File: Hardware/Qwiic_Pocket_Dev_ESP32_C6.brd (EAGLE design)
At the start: 25.4 x 25.4 mm, 94 parts, among them J1 USB Female Type C Connector, J4 QWIIC_RIGHT_ANGLE, Q1 20V/4.2A/52mΩ/1.4W, U1 ESP32-C6-MINI-1, U2 RT9080-33GJ5, U3 MCP73831

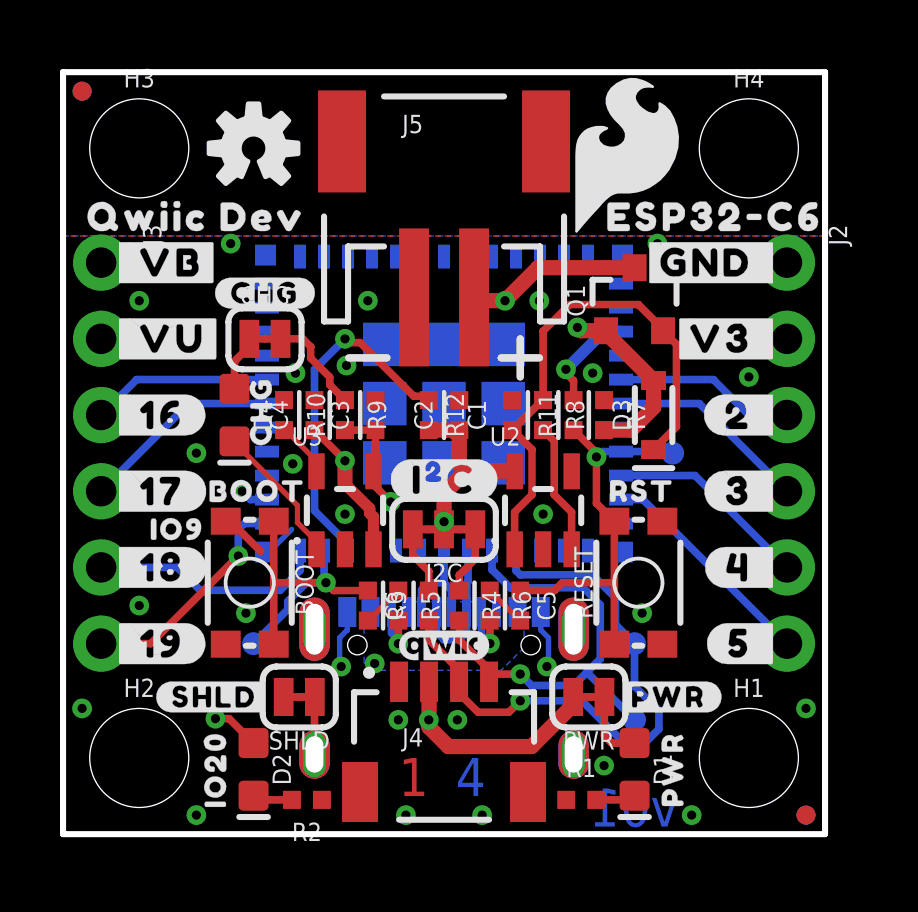
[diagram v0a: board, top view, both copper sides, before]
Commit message: Move fiducials
Moved inward to make it easier for PnP to handle single boards
Decided to flip the fiducial corners, made it easier to move inwards
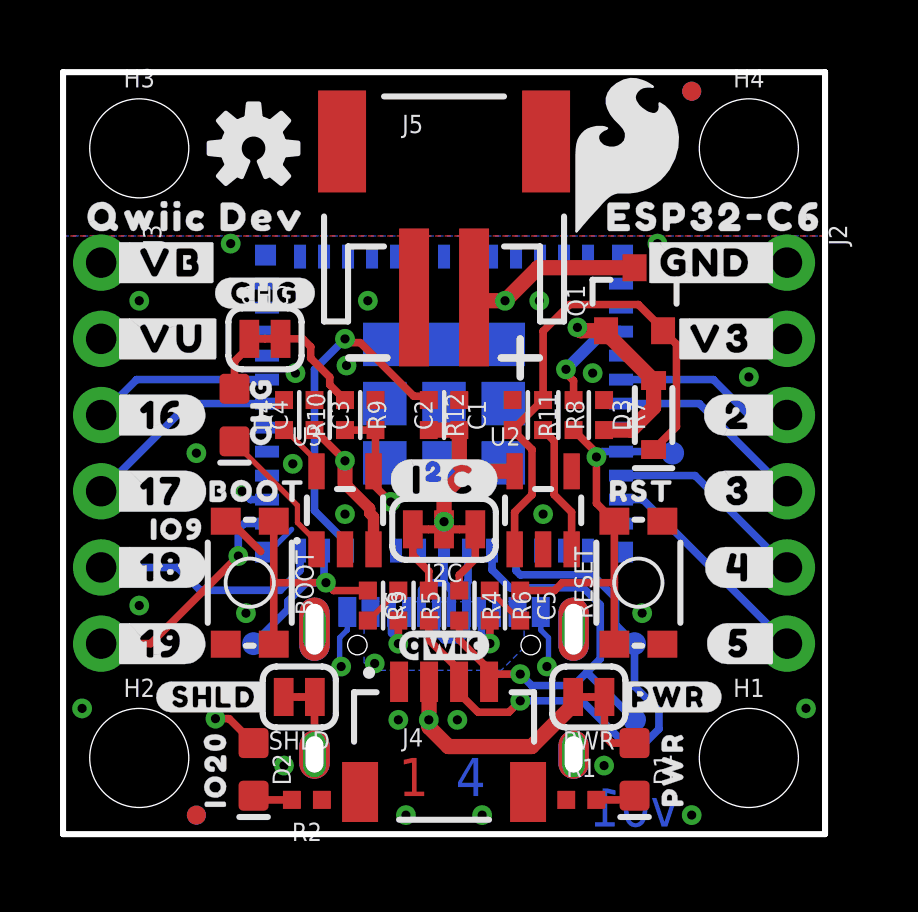
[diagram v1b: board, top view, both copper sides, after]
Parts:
- moved FD3 20.3 mm to (4.45, 0.64)
- moved FD4 20.3 mm to (4.45, 0.64)
- moved FD1 20.3 mm to (21.0, 24.8)
- moved FD2 20.3 mm to (21.0, 24.8)
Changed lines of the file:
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@@
 <element name="U$10" library="SparkFun-Aesthetics" package="SFE_LOGO_FLAME_.1" value="" x="6.35" y="2.54" smashed="yes" rot="MR0"/>
 <element name="U$11" library="output" package="ESP32#C633" value="" x="4.064" y="4.826" smashed="yes" rot="MR0"/>
-<element name="FD1" library="SparkFun-Aesthetics" package="FIDUCIAL-MICRO" value="FIDUCIALUFIDUCIAL" x="0.635" y="24.765" smashed="yes" rot="MR0"/>
-<element name="FD2" library="SparkFun-Aesthetics" package="FIDUCIAL-MICRO" value="FIDUCIALUFIDUCIAL" x="0.635" y="24.765" smashed="yes"/>
-<element name="FD3" library="SparkFun-Aesthetics" package="FIDUCIAL-MICRO" value="FIDUCIALUFIDUCIAL" x="24.765" y="0.635" smashed="yes" rot="MR0"/>
-<element name="FD4" library="SparkFun-Aesthetics" package="FIDUCIAL-MICRO" value="FIDUCIALUFIDUCIAL" x="24.765" y="0.635" smashed="yes"/>
+<element name="FD1" library="SparkFun-Aesthetics" package="FIDUCIAL-MICRO" value="FIDUCIALUFIDUCIAL" x="20.955" y="24.765" smashed="yes" rot="MR0"/>
+<element name="FD2" library="SparkFun-Aesthetics" package="FIDUCIAL-MICRO" value="FIDUCIALUFIDUCIAL" x="20.955" y="24.765" smashed="yes"/>
+<element name="FD3" library="SparkFun-Aesthetics" package="FIDUCIAL-MICRO" value="FIDUCIALUFIDUCIAL" x="4.445" y="0.635" smashed="yes" rot="MR0"/>
+<element name="FD4" library="SparkFun-Aesthetics" package="FIDUCIAL-MICRO" value="FIDUCIALUFIDUCIAL" x="4.445" y="0.635" smashed="yes"/>
 <element name="U$12" library="output" package="ESP32#C633" value="" x="21.717" y="20.574" smashed="yes"/>
 <element name="U$23" library="output" package="#I�C#0" value="" x="12.7" y="11.811" smashed="yes"/>
@@
 <wire x1="16.1817" y1="5.6407" x2="16.1817" y2="6.54709375" width="0.1778" layer="16"/>
 <via x="20.955" y="0.635" extent="1-16" drill="0.3048"/>
-<via x="4.445" y="0.635" extent="1-16" drill="0.3048"/>
+<via x="7.366" y="2.286" extent="1-16" drill="0.3048"/>
 <wire x1="11.176" y1="8.12" x2="10.176" y2="7.12" width="0.1778" layer="1"/>
 <wire x1="10.176" y1="7.12" x2="10.16" y2="7.12" width="0.1778" layer="1"/>

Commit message: Add battery voltage divider
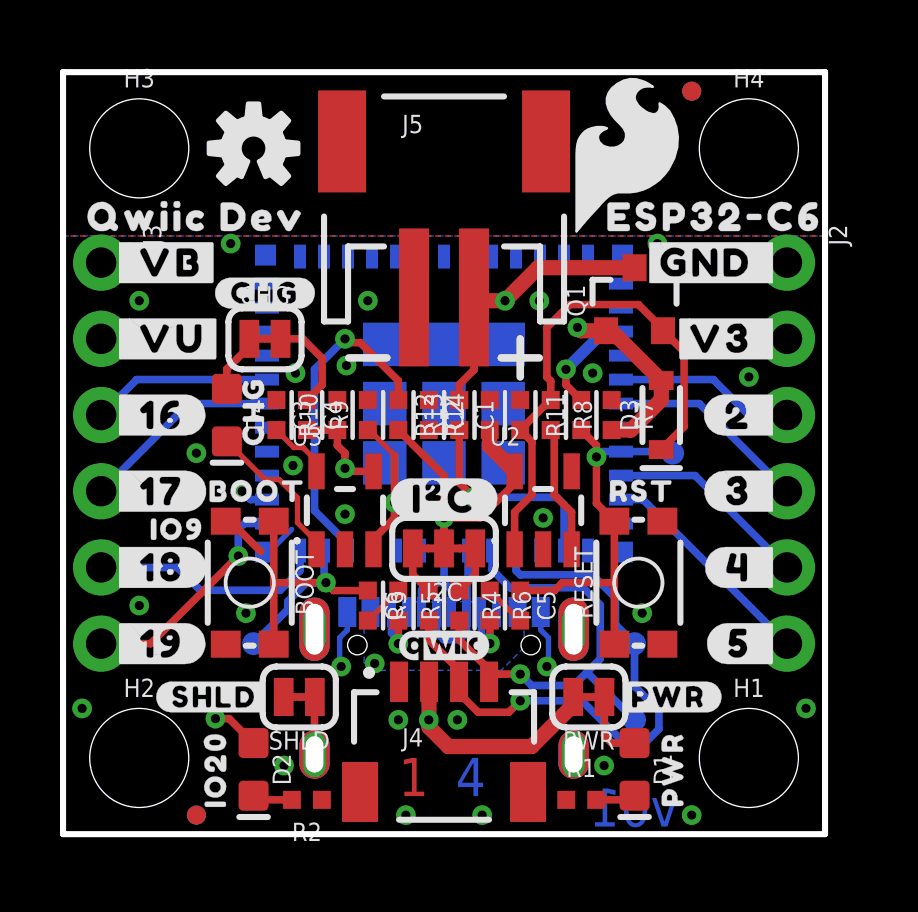
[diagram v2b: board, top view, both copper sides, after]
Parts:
- added R13, R14: 100k, SparkFun-Resistors:0402-TIGHT
- moved C4 1.78 mm to (10.2, 14.0)
- moved C3 1.27 mm to (9.14, 14.0)
- moved R9 1.27 mm to (8.13, 14.0)
- moved C2 1.02 mm to (14.2, 14.0)
- moved R12 1.02 mm to (11.2, 14.0)
- moved I2C 0.63 mm to (12.7, 9.53)
- moved U$23 0.63 mm to (12.7, 11.2)
- moved D3 0.25 mm to (19.9, 14.0)
- moved R7 0.25 mm to (18.3, 14.0)
- moved R8 0.25 mm to (16.3, 14.0)
- moved U$32 0.25 mm to (6.35, 14.1)
- moved C1 0.25 mm to (15.2, 14.0)
- moved D4 0.25 mm to (5.46, 14.0)
- moved R10 0.25 mm to (7.11, 14.0)
- moved R11 0.25 mm to (17.3, 14.0)
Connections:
- new net IO1/V_BATT_2: R13.1, R14.2, U1.13
- net GND: now also R14.1
- net V_BATT: now also R13.2
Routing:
- net IO1/V_BATT_2: track 0.00 -> 8.10 mm, vias 0 -> 1
- net V_BATT: track 30.1 -> 34.8 mm
- net 3.3V: track 38.7 -> 43.0 mm
- net N$14: track 11.6 -> 10.9 mm
- net N$5: track 2.26 -> 1.63 mm
- net N$4: track 2.26 -> 1.63 mm
